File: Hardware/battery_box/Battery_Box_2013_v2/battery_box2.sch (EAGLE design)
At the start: 49 parts, among them IC1 AD826R, IC2 LM2574, IC3 PIC16F1824, IC4 LD117AS18TR, J1 CON_HEADER_PRG_PIC_ICSPA, Q1 IRFR5505PBFTO252, Q2 BSS123, X1 CON_MOLEX_39_29_1028, X2 KUSBVX

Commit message: added pdf of schematic
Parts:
- C3: value 22u -> 220u
- C6: device resistor:C-EUC0805 -> rcl:C-EUC0402
- R14, R15: value 66k -> 66k5
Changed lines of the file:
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@@
 <?xml version="1.0" encoding="utf-8"?>
 <!DOCTYPE eagle SYSTEM "eagle.dtd">
-<eagle version="6.3">
+<eagle version="6.4">
 <drawing>
 <settings>
@@
 <part name="IC2" library="equinox" deviceset="LM2574" device=""/>
 <part name="C2" library="rcl" deviceset="C-EU" device="C0805" value="22u"/>
-<part name="C3" library="rcl" deviceset="C-EU" device="C0805" value="22u"/>
+<part name="C3" library="rcl" deviceset="C-EU" device="C0805" value="220u"/>
 <part name="L1" library="equinox" deviceset="INDUCTOR" device=""/>
 <part name="Q1" library="equinox" deviceset="IRFR5505PBF" device="TO252"/>
@@
 <part name="R12" library="rcl" deviceset="R-EU_" device="R0805" value="100k"/>
 <part name="R13" library="rcl" deviceset="R-EU_" device="R0805" value="100k"/>
-<part name="R14" library="rcl" deviceset="R-EU_" device="R0805" value="66k"/>
-<part name="R15" library="rcl" deviceset="R-EU_" device="R0805" value="66k"/>
+<part name="R14" library="rcl" deviceset="R-EU_" device="R0805" value="66k5"/>
+<part name="R15" library="rcl" deviceset="R-EU_" device="R0805" value="66k5"/>
 <part name="R16" library="rcl" deviceset="R-EU_" device="R0805" value="20k"/>
 <part name="R17" library="rcl" deviceset="R-EU_" device="R0805" value="20k"/>
@@
 <part name="C5" library="rcl" deviceset="C-EU" device="C1210" value="10u, 25V"/>
 <part name="D1" library="diode" deviceset="SCHOTTKY-DIODE" device="SMD"/>
-<part name="C6" library="resistor" deviceset="C-EU" device="C0805" value="100n"/>
+<part name="C6" library="rcl" deviceset="C-EU" device="C0402" value="100n"/>
 </parts>
 <sheets>

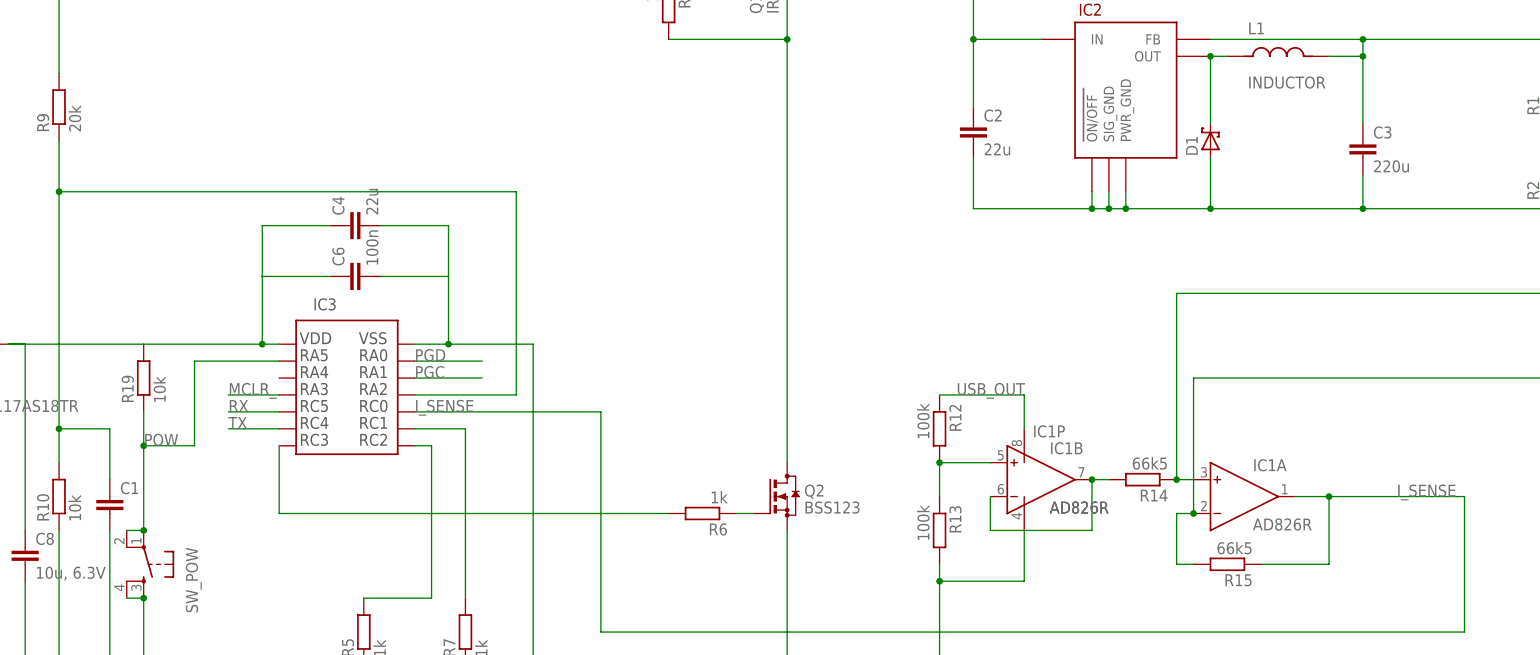
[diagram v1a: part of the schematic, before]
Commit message: updated C3 footprint and component values/cost
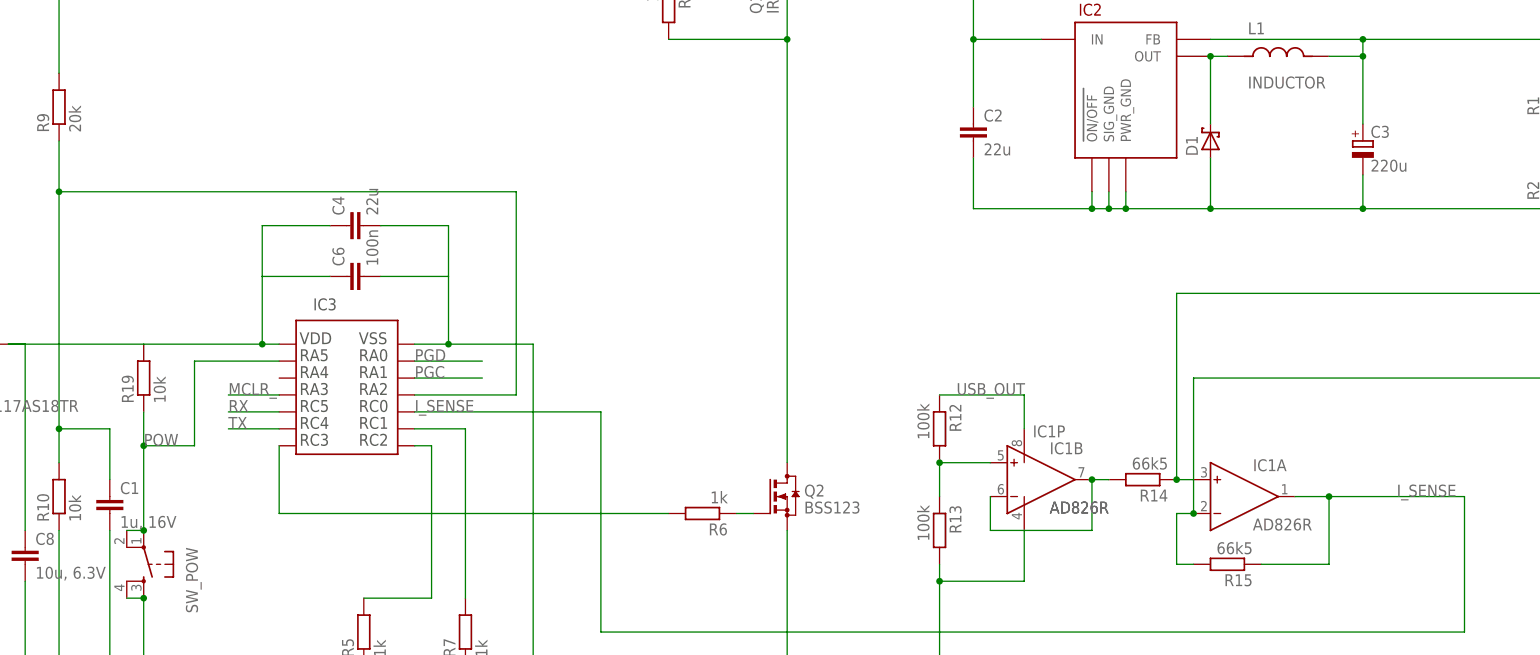
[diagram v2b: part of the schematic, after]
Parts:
- C1: value (none) -> 1u, 16V
- C2: device rcl:C-EUC0805 -> rcl:C-EUC1210
- C3: device rcl:C-EUC0805 -> rcl:CPOL-EUE
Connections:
- net GND_OUTPUT: now also C3.-; no longer C3.2
- net USB_OUT: now also C3.+; no longer C3.1
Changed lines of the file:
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@@
 <part name="R9" library="rcl" deviceset="R-EU_" device="R0805" value="20k"/>
 <part name="R10" library="rcl" deviceset="R-EU_" device="R0805" value="10k"/>
-<part name="C1" library="rcl" deviceset="C-EU" device="C0805"/>
+<part name="C1" library="rcl" deviceset="C-EU" device="C0805" value="1u, 16V"/>
 <part name="IC2" library="equinox" deviceset="LM2574" device=""/>
-<part name="C2" library="rcl" deviceset="C-EU" device="C0805" value="22u"/>
-<part name="C3" library="rcl" deviceset="C-EU" device="C0805" value="220u"/>
+<part name="C2" library="rcl" deviceset="C-EU" device="C1210" value="22u"/>
+<part name="C3" library="rcl" deviceset="CPOL-EU" device="E" value="220u"/>
 <part name="L1" library="equinox" deviceset="INDUCTOR" device=""/>
 <part name="Q1" library="equinox" deviceset="IRFR5505PBF" device="TO252"/>
@@
 <net name="USB_OUT" class="0">
 <segment>
-<pinref part="C3" gate="G$1" pin="1"/>
+<pinref part="C3" gate="G$1" pin="+"/>
 <pinref part="IC2" gate="G$1" pin="FB"/>
 <wire x1="264.16" y1="152.4" x2="264.16" y2="162.56" width="0.1524" layer="91"/>
@@
 <wire x1="345.44" y1="165.1" x2="347.98" y2="165.1" width="0.1524" layer="91"/>
 <junction x="345.44" y="165.1"/>
-<pinref part="C3" gate="G$1" pin="2"/>
+<pinref part="C3" gate="G$1" pin="-"/>
 <wire x1="264.16" y1="139.7" x2="264.16" y2="144.78" width="0.1524" layer="91"/>
 <pinref part="IC2" gate="G$1" pin="PWR_GND"/>

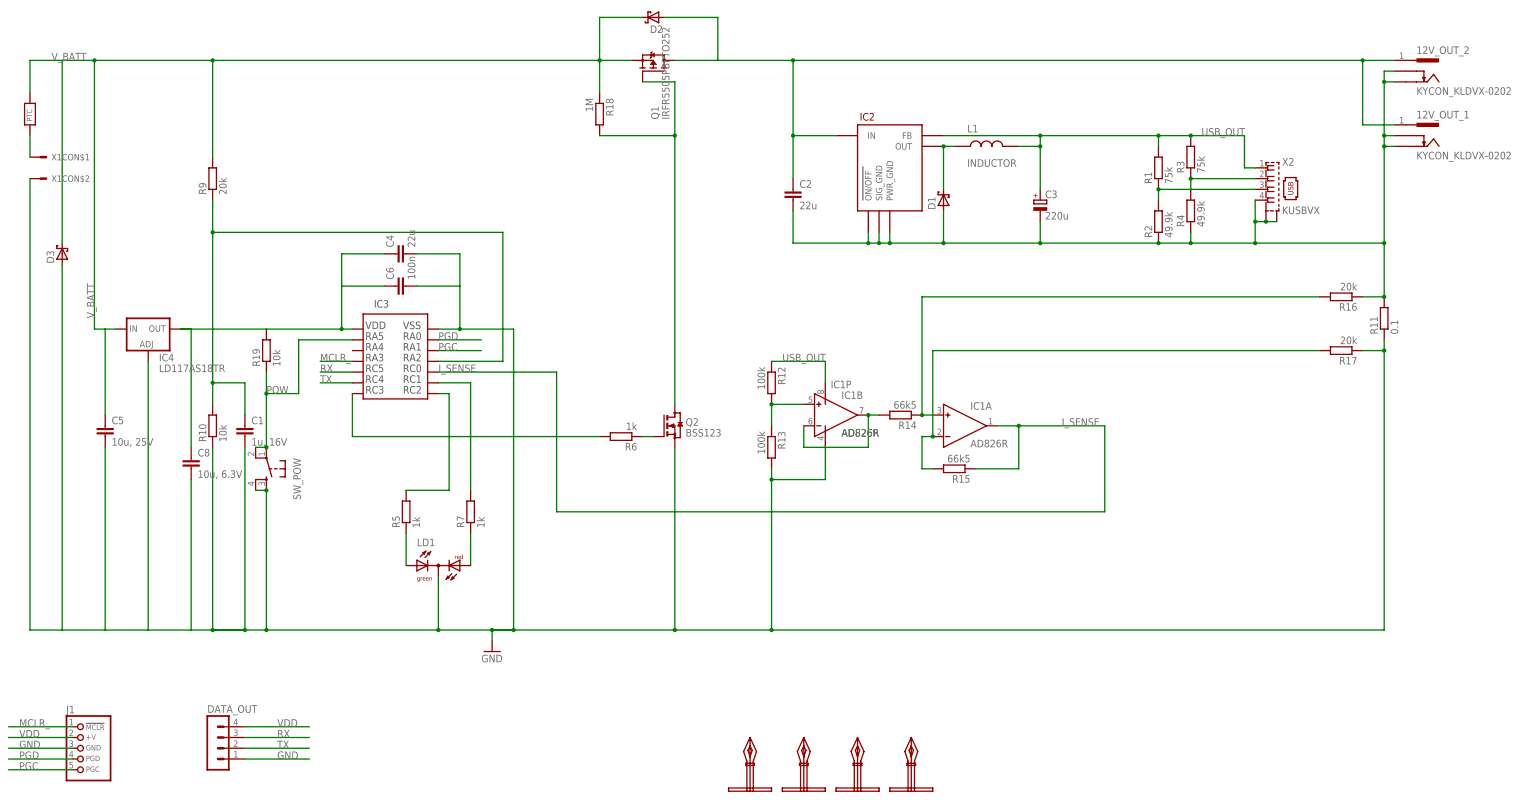
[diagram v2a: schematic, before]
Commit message: Most recent Gerbers
Most recent footprints and testpoints added.
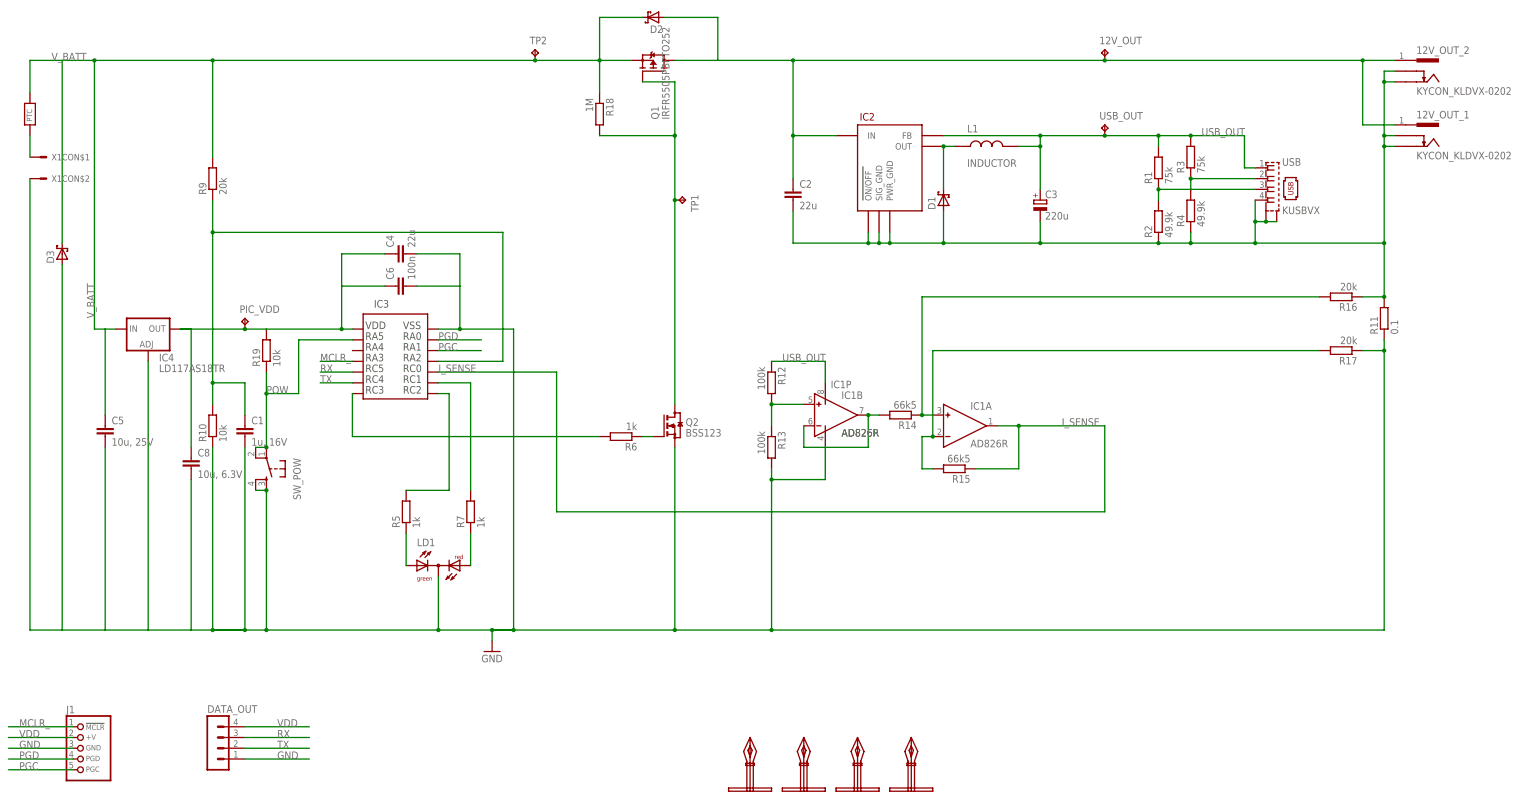
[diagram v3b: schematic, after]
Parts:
- added 12V_OUT, USB_OUT: TPTP20R, testpad:TPTP20R
- added PIC_VDD, TP1, TP2: TPTP14R, testpad:TPTP14R
- renumbered X2 to USB
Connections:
- net 12V_OUT: now also 12V_OUT.TP
- net N$11: now also TP1.TP
- net USB_OUT: now also USB_OUT.TP
- net VDD: now also PIC_VDD.TP
- net V_BATT: now also TP2.TP
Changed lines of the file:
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@@
 <part name="12V_OUT_2" library="equinox" deviceset="KYCON_KLDVX-0202" device=""/>
 <part name="12V_OUT_1" library="equinox" deviceset="KYCON_KLDVX-0202" device=""/>
-<part name="X2" library="con-kycon" deviceset="KUSBVX" device=""/>
+<part name="USB" library="con-kycon" deviceset="KUSBVX" device=""/>
 <part name="LD1" library="led" deviceset="DUOLED-RG-C" device=""/>
 <part name="J1" library="equinox" deviceset="CON_HEADER_PRG_PIC_ICSP" device="A"/>
@@
 <part name="D1" library="diode" deviceset="SCHOTTKY-DIODE" device="SMD"/>
 <part name="C6" library="rcl" deviceset="C-EU" device="C0402" value="100n"/>
+<part name="USB_OUT" library="testpad" deviceset="TP" device="TP20R"/>
+<part name="12V_OUT" library="testpad" deviceset="TP" device="TP20R"/>
+<part name="PIC_VDD" library="testpad" deviceset="TP" device="TP14R" value="TPTP14R"/>
+<part name="TP1" library="testpad" deviceset="TP" device="TP14R" value="TPTP14R"/>
+<part name="TP2" library="testpad" deviceset="TP" device="TP14R" value="TPTP14R"/>
 </parts>
 <sheets>
@@
 <instance part="12V_OUT_2" gate="G$1" x="355.6" y="180.34"/>
 <instance part="12V_OUT_1" gate="G$1" x="355.6" y="165.1"/>
-<instance part="X2" gate="G$1" x="320.04" y="152.4"/>
+<instance part="USB" gate="G$1" x="320.04" y="152.4"/>
 <instance part="LD1" gate="G$1" x="121.92" y="63.5" rot="MR90"/>
 <instance part="J1" gate="J" x="38.1" y="20.32"/>
@@
 <instance part="D1" gate="G$1" x="241.3" y="149.86" rot="R90"/>
 <instance part="C6" gate="G$1" x="111.76" y="129.54" rot="R90"/>
+<instance part="USB_OUT" gate="G$1" x="279.4" y="167.64"/>
+<instance part="12V_OUT" gate="G$1" x="279.4" y="185.42"/>
+<instance part="PIC_VDD" gate="G$1" x="76.2" y="121.92"/>
+<instance part="TP1" gate="G$1" x="180.34" y="149.86" rot="R270"/>
+<instance part="TP2" gate="G$1" x="144.78" y="185.42"/>
 </instances>
 <busses>
@@
 <pinref part="IC4" gate="G$1" pin="OUT"/>
 <wire x1="99.06" y1="129.54" x2="99.06" y2="119.38" width="0.1524" layer="91"/>
-<wire x1="60.96" y1="119.38" x2="81.28" y2="119.38" width="0.1524" layer="91"/>
+<wire x1="60.96" y1="119.38" x2="76.2" y2="119.38" width="0.1524" layer="91"/>
+<wire x1="76.2" y1="119.38" x2="81.28" y2="119.38" width="0.1524" layer="91"/>
 <wire x1="109.22" y1="129.54" x2="99.06" y2="129.54" width="0.1524" layer="91"/>
 <pinref part="C8" gate="G$1" pin="1"/>
@@
 <wire x1="63.5" y1="119.38" x2="60.96" y2="119.38" width="0.1524" layer="91"/>
 <pinref part="C6" gate="G$1" pin="1"/>
+<pinref part="PIC_VDD" gate="G$1" pin="TP"/>
+<junction x="76.2" y="119.38"/>
 </segment>
 <segment>
@@
 <junction x="40.64" y="182.88"/>
 <pinref part="U$2" gate="G$1" pin="P$2"/>
-<wire x1="160.02" y1="182.88" x2="68.58" y2="182.88" width="0.1524" layer="91"/>
+<wire x1="160.02" y1="182.88" x2="144.78" y2="182.88" width="0.1524" layer="91"/>
+<wire x1="144.78" y1="182.88" x2="68.58" y2="182.88" width="0.1524" layer="91"/>
 <wire x1="68.58" y1="182.88" x2="40.64" y2="182.88" width="0.1524" layer="91"/>
 <wire x1="25.4" y1="175.26" x2="25.4" y2="182.88" width="0.1524" layer="91"/>
@@
 <wire x1="43.18" y1="119.38" x2="40.64" y2="119.38" width="0.1524" layer="91"/>
 <wire x1="43.18" y1="99.06" x2="43.18" y2="119.38" width="0.1524" layer="91"/>
+<pinref part="TP2" gate="G$1" pin="TP"/>
+<junction x="144.78" y="182.88"/>
 </segment>
 </net>
@@
 <wire x1="259.08" y1="162.56" x2="264.16" y2="162.56" width="0.1524" layer="91"/>
 <junction x="264.16" y="162.56"/>
-<wire x1="292.1" y1="165.1" x2="264.16" y2="165.1" width="0.1524" layer="91"/>
+<wire x1="292.1" y1="165.1" x2="279.4" y2="165.1" width="0.1524" layer="91"/>
 <junction x="264.16" y="165.1"/>
 <pinref part="R1" gate="G$1" pin="2"/>
 <pinref part="R3" gate="G$1" pin="2"/>
-<pinref part="X2" gate="G$1" pin="1"/>
+<pinref part="USB" gate="G$1" pin="1"/>
+<wire x1="279.4" y1="165.1" x2="264.16" y2="165.1" width="0.1524" layer="91"/>
 <wire x1="314.96" y1="157.48" x2="312.42" y2="157.48" width="0.1524" layer="91"/>
 <wire x1="312.42" y1="157.48" x2="312.42" y2="165.1" width="0.1524" layer="91"/>
@@
 <label x="302.26" y="165.1" size="1.778" layer="95"/>
 <junction x="292.1" y="165.1"/>
+<pinref part="USB_OUT" gate="G$1" pin="TP"/>
+<junction x="279.4" y="165.1"/>
 </segment>
 <segment>
@@
 <pinref part="R2" gate="G$1" pin="2"/>
 <wire x1="292.1" y1="152.4" x2="292.1" y2="149.86" width="0.1524" layer="91"/>
-<pinref part="X2" gate="G$1" pin="3"/>
+<pinref part="USB" gate="G$1" pin="3"/>
 <wire x1="314.96" y1="152.4" x2="292.1" y2="152.4" width="0.1524" layer="91"/>
 <junction x="292.1" y="152.4"/>
@@
 <pinref part="R3" gate="G$1" pin="1"/>
 <wire x1="299.72" y1="152.4" x2="299.72" y2="154.94" width="0.1524" layer="91"/>
-<pinref part="X2" gate="G$1" pin="2"/>
+<pinref part="USB" gate="G$1" pin="2"/>
 <wire x1="299.72" y1="154.94" x2="314.96" y2="154.94" width="0.1524" layer="91"/>
 <junction x="299.72" y="154.94"/>
@@
 <wire x1="177.8" y1="177.8" x2="177.8" y2="165.1" width="0.1524" layer="91"/>
 <pinref part="R18" gate="G$1" pin="2"/>
-<wire x1="177.8" y1="165.1" x2="177.8" y2="101.6" width="0.1524" layer="91"/>
+<wire x1="177.8" y1="165.1" x2="177.8" y2="149.86" width="0.1524" layer="91"/>
+<wire x1="177.8" y1="149.86" x2="177.8" y2="101.6" width="0.1524" layer="91"/>
 <wire x1="160.02" y1="165.1" x2="177.8" y2="165.1" width="0.1524" layer="91"/>
 <junction x="177.8" y="165.1"/>
+<pinref part="TP1" gate="G$1" pin="TP"/>
+<junction x="177.8" y="149.86"/>
 </segment>
 </net>
@@
 <wire x1="177.8" y1="182.88" x2="187.96" y2="182.88" width="0.1524" layer="91"/>
 <wire x1="187.96" y1="182.88" x2="205.74" y2="182.88" width="0.1524" layer="91"/>
-<wire x1="205.74" y1="182.88" x2="340.36" y2="182.88" width="0.1524" layer="91"/>
+<wire x1="205.74" y1="182.88" x2="279.4" y2="182.88" width="0.1524" layer="91"/>
+<wire x1="279.4" y1="182.88" x2="340.36" y2="182.88" width="0.1524" layer="91"/>
 <wire x1="215.9" y1="165.1" x2="205.74" y2="165.1" width="0.1524" layer="91"/>
 <wire x1="205.74" y1="165.1" x2="205.74" y2="182.88" width="0.1524" layer="91"/>
@@
 <pinref part="D2" gate="G$1" pin="A"/>
 <wire x1="187.96" y1="193.04" x2="175.26" y2="193.04" width="0.1524" layer="91"/>
+<pinref part="12V_OUT" gate="G$1" pin="TP"/>
+<junction x="279.4" y="182.88"/>
 </segment>
 </net>
 <net name="GND_OUTPUT" class="1">
 <segment>
-<pinref part="X2" gate="G$1" pin="S2"/>
-<pinref part="X2" gate="G$1" pin="S1"/>
+<pinref part="USB" gate="G$1" pin="S2"/>
+<pinref part="USB" gate="G$1" pin="S1"/>
 <junction x="317.5" y="144.78"/>
 <wire x1="317.5" y1="144.78" x2="320.04" y2="144.78" width="0.1524" layer="91"/>
-<pinref part="X2" gate="G$1" pin="4"/>
+<pinref part="USB" gate="G$1" pin="4"/>
 <wire x1="314.96" y1="149.86" x2="314.96" y2="144.78" width="0.1524" layer="91"/>
 <wire x1="314.96" y1="144.78" x2="317.5" y2="144.78" width="0.1524" layer="91"/>
